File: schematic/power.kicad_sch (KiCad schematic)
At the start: 17 parts, among them SW1 SW_MEC_5E, U2 LSM6DSO32TR, U3 AP2210N-3.3TRG1

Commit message: Complete schematic
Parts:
- added D6: LED, LED_SMD:LED_0603_1608Metric_Pad1.05x0.95mm_HandSolder, symbol Device:LED
- added R12: 220R, Resistor_SMD:R_0603_1608Metric, symbol Device:R
- C10, C11: footprint (none) -> Capacitor_SMD:C_0402_1005Metric
- C8, C9: footprint (none) -> Capacitor_SMD:C_0603_1608Metric
- D1, D2, D3, D4: footprint (none) -> LED_SMD:LED_0603_1608Metric
- R10, R11, R2, R3, R4, R5: footprint (none) -> Resistor_SMD:R_0603_1608Metric
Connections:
- net GND: now also D6.1 (K)
- new net: D6.2 (A), R12.2
- new net LED_SAT3: R12.1

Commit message: Minor fixes.
D6 footprint, updated BOM
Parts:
- D6: footprint LED_SMD:LED_0603_1608Metric_Pad1.05x0.95mm_HandSolder -> LED_SMD:LED_0603_1608Metric
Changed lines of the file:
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@@
       (effects (font (size 1.27 1.27)) (justify right))
     )
-    (property "Footprint" "LED_SMD:LED_0603_1608Metric_Pad1.05x0.95mm_HandSolder" (id 2) (at 111.76 146.05 0)
+    (property "Footprint" "LED_SMD:LED_0603_1608Metric" (id 2) (at 111.76 146.05 0)
       (effects (font (size 1.27 1.27)) hide)
     )

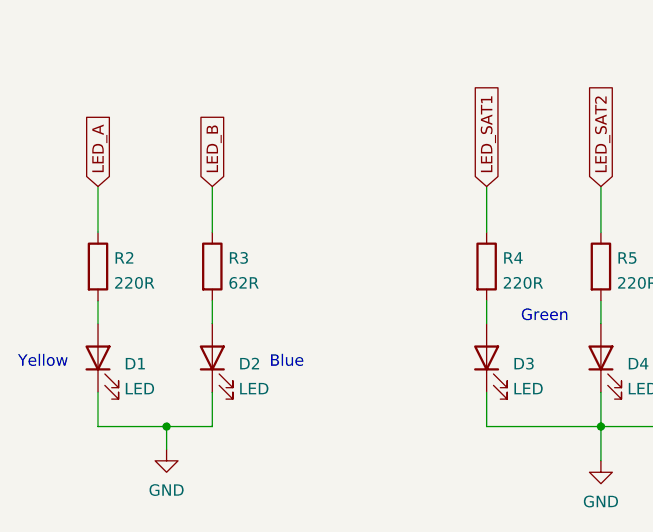
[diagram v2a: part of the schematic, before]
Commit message: Changed R3 value and some minor track adjustments
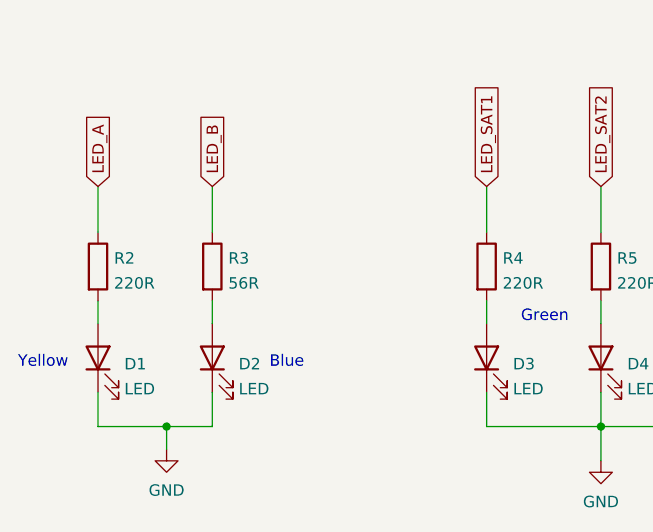
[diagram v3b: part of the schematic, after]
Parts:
- R3: value 62R -> 56R
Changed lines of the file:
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@@
       (effects (font (size 1.27 1.27)) (justify left))
     )
-    (property "Value" "62R" (id 1) (at 57.658 137.7566 0)
+    (property "Value" "56R" (id 1) (at 57.658 137.7566 0)
       (effects (font (size 1.27 1.27)) (justify left))
     )
